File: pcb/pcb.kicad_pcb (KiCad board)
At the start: 2 copper layers, 350 x 170 mm, 79 parts, among them J1 Conn_01x24, SW1 0, SW10 9, SW11 HYPHEN, SW12 CARET, SW13 YEN, SW14 AT, SW15 LBRACKET, SW16 SEMICOLON, SW17 COLON, SW18 RBRACKET, SW19 COMMA, SW2 1, SW20 FULLSTOP, SW21 SLASH, SW22 UNDERSCORE, SW23 A, SW24 B, SW25 C, SW26 D, SW27 E, SW28 F, SW29 G, SW3 2, SW30 H, SW31 I, SW32 J, SW33 K, SW34 L, SW35 M, SW36 N, SW37 O, SW38 P, SW39 Q, SW4 3, SW40 R, SW41 PAUSE, SW42 S, SW43 T, SW44 U, SW45 V, SW46 W, SW47 X, SW48 Y, SW49 Z, SW5 4, SW50 LSHIFT, SW51 CTRL, SW52 GRAPH, SW53 CAP, SW54 KANA, SW55 F1/F6, SW56 F2/F7, SW57 F3/F8, SW58 RSHIFT, SW59 F4/F9, SW6 5, SW60 F5/F10, SW61 ESC, SW62 TAB, SW63 STOP, SW64 BS, SW65 SELECT, SW66 RETURN, SW67 SPACE, SW68 HOME, SW69 INS, SW7 6, SW70 DEL, SW71 LEFT, SW72 UP, SW73 DOWN, SW74 RIGHT, SW8 7, SW9 8

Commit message: PCB via fiducials and routing optimisations
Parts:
- turned SW64 to 45 degrees
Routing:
- net /6: track 520.4 -> 559.5 mm
- net /8: track 698.8 -> 706.0 mm
- net /17: track 473.1 -> 466.1 mm
- net /5: track 1030.1 -> 1023.3 mm
- net /9: track 765.8 -> 759.1 mm
- net /16: track 411.7 -> 418.2 mm
- net /12: track 769.5 -> 767.4 mm
- net /1: track 694.7 -> 695.6 mm
- net /7: track 692.4 -> 691.8 mm, vias 6 -> 5
- net Net-(J1-Pin_22): track 247.3 -> 246.7 mm

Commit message: Reviewing PCB and updating switch spacing
Changed soldermask layer on the connector to not be along the whole
trace. Reviewed the pinout of all the switches and confirmed they're
good. Reviewed the spacing of the switches and found errors, I have
moved them but am yet to reroute the traces. Updated the teardrops to be
curved.
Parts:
- removed SYM1: Logo_Open_Hardware_Small, Symbol:OSHW-Logo_5.7x6mm_SilkScreen
- added FID3: Fiducial, Fiducial:Fiducial_1mm_Mask2mm, F.Cu at (35.5, 211.0)
- added FID4: Fiducial, Fiducial:Fiducial_1mm_Mask2mm, B.Cu at (381.5, 211.0)
- FID1: moved to B.Cu
- moved FID1 110.0 mm to (35.5, 101.0), turned to 180 degrees
- moved SW11 0.54 mm to (260.7, 124.4)
- moved SW12 0.54 mm to (279.7, 124.4)
- moved SW13 0.54 mm to (298.8, 124.4)
- moved SW8 0.54 mm to (184.5, 124.4)
- moved SW4 0.54 mm to (108.3, 124.4)
- moved SW5 0.54 mm to (127.3, 124.4)
- moved SW1 0.54 mm to (241.6, 124.4)
- moved SW10 0.54 mm to (222.6, 124.4)
- moved SW2 0.54 mm to (70.2, 124.4)
- moved SW3 0.54 mm to (89.2, 124.4)
- moved SW6 0.54 mm to (146.4, 124.4)
- moved SW7 0.54 mm to (165.4, 124.4)
- moved SW9 0.54 mm to (203.5, 124.4)
- moved SW64 0.54 mm to (317.8, 124.4)
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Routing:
- net /16: track 418.2 -> 293.9 mm
- net /5: track 1023.3 -> 914.5 mm
- net /11: track 616.4 -> 509.1 mm, vias 6 -> 5
- net /1: track 695.6 -> 608.1 mm
- net /15: track 422.5 -> 349.9 mm, vias 5 -> 4
- net /4: track 256.2 -> 184.1 mm, vias 4 -> 3
- net /9: track 759.1 -> 692.5 mm
- net /13: track 690.9 -> 625.2 mm, vias 5 -> 4
- net /3: track 388.7 -> 325.7 mm
- net /14: track 296.4 -> 247.7 mm, vias 2 -> 1
- net /2: track 703.7 -> 663.0 mm, vias 6 -> 5
- net /10: track 583.9 -> 545.4 mm, vias 6 -> 5
- net /7: track 691.8 -> 663.6 mm
- net /17: track 466.1 -> 442.5 mm
- net /12: track 767.4 -> 745.4 mm, vias 6 -> 5
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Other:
- outline, holes or cut-outs redrawn
- rule pad_to_mask_clearance: 0 -> 0.1
- board text added: "1"
- board text added: "2"

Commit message: Rerouted the deleted traces
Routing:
- net /16: track 293.9 -> 408.0 mm
- net /5: track 914.5 -> 1023.7 mm
- net /11: track 509.1 -> 617.8 mm, vias 5 -> 6
- net /1: track 608.1 -> 698.3 mm
- net /15: track 349.9 -> 424.5 mm, vias 4 -> 5
- net /4: track 184.1 -> 258.3 mm, vias 3 -> 4
- net /13: track 625.2 -> 692.7 mm, vias 4 -> 5
- net /9: track 692.5 -> 756.7 mm
- net /3: track 325.7 -> 387.2 mm
- net /14: track 247.7 -> 299.2 mm, vias 1 -> 2
- net /2: track 663.0 -> 705.2 mm, vias 5 -> 6
- net /10: track 545.4 -> 580.4 mm, vias 5 -> 6
- net /7: track 663.6 -> 689.7 mm
- net /17: track 442.5 -> 466.5 mm
- net /12: track 745.4 -> 769.0 mm, vias 5 -> 6
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
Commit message: Adding stiffener and fab notes
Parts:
- moved D1 25.0 mm to (365.1, 129.0)
- moved FID1 25.0 mm to (35.5, 126.0)
- moved FID2 25.0 mm to (381.5, 126.5)
- moved FID3 25.0 mm to (35.5, 236.0)
- moved FID4 25.0 mm to (381.5, 236.0)
- moved J1 25.0 mm to (300.3, 86.5)
- moved SW1 25.0 mm to (241.6, 149.4)
- moved SW10 25.0 mm to (222.6, 149.4)
- moved SW11 25.0 mm to (260.7, 149.4)
- moved SW12 25.0 mm to (279.7, 149.4)
- moved SW13 25.0 mm to (298.8, 149.4)
- moved SW14 25.0 mm to (270.2, 168.4)
- moved SW15 25.0 mm to (289.3, 168.4)
- moved SW16 25.0 mm to (255.9, 187.5)
- moved SW17 25.0 mm to (275.0, 187.5)
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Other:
- rule pad_to_mask_clearance: 0.1 -> 0
- board text added: "0 mm"
- board text added: "0.0117 mm"
- board text added: "0.025 mm"
- board text added: "0.0254 um (1 u{dblquote})"
- board text added: "0.0275 mm"
- board text added: "0.1100 mm"
- board text added: "0.2500 mm"
- board text added: "0.2500 mm / 0.2500 mm"
- board text added: "0.3100 mm"
- board text added: "0.5000 mm"
- board text added: "12 um finish copper (1/3 Oz.)"
- board text added: "350.0000 mm x 170.0000 mm"
- board text added: "65.0000 mm x 15.0000 mm"
- board text added: "B.Cu"
- board text added: "B.Mask"
- board text added: "B.Paste"
- board text added: "B.Silkscreen"
- board text added: "B.Stiffener"
- board text added: "BOARD CHARACTERISTICS"
- board text added: "Blind and buried vias:"
- board text added: "Board Thickness:"
- board text added: "Board overall dimensions:"
- board text added: "Bottom Silk Screen"
- board text added: "Bottom Solder Mask"
- board text added: "Bottom Solder Paste"
- board text added: "Bottom Stiffener"
- board text added: "Castellated pads:"
- board text added: "Color"
- board text added: "Copper Finish:"
- board text added: "Copper Layer Count:"
- board text added: "Copper Thickness:"
- board text added: "Coverlay"
- board text added: "Cut-out in design:"
- board text added: "Dielectric 1"
- board text added: "Direct Printing"
- board text added: "ENIG"
- board text added: "Edge card connectors:"
- board text added: "F.Cu"
- board text added: "F.Mask"
- board text added: "F.Paste"
- board text added: "F.Silkscreen"
- board text added: "Gerber layer:"
- board text added: "Impedance Control:"
- board text added: "Layer Name"
- board text added: "Material"
- board text added: "Material:"
- board text added: "Min hole diameter:"
- board text added: "Min track/spacing:"
- board text added: "Minimum plating thickness:"
- board text added: "No"
- board text added: "Plated Board Edge:"
- board text added: "Polyimide"
- board text added: "STIFFENER CHARACTERISTICS"
- board text added: "Stiffener Thickness:"
- board text added: "Stiffener overall dimensions:"
- board text added: "Stiffener required:"
- board text added: "Tented"
- board text added: "Thickness (mm)"
- board text added: "Top Silk Screen"
- board text added: "Top Solder Mask"
- board text added: "Top Solder Paste"
- board text added: "Total Thickness:"
- board text added: "Type"
- board text added: "User.1"
- board text added: "Via covering:"
- board text added: "Via in pad:"
- board text added: "White"
- board text added: "Yellow"
- board text added: "Yes"
- board text added: "copper"
- board text added: "core"

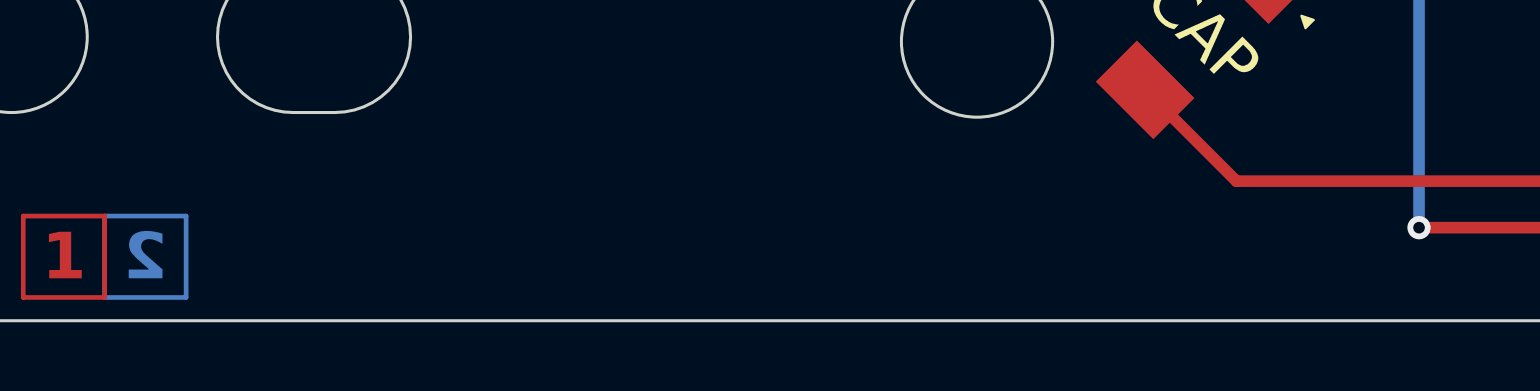
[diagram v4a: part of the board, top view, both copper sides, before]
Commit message: Adding serial number label
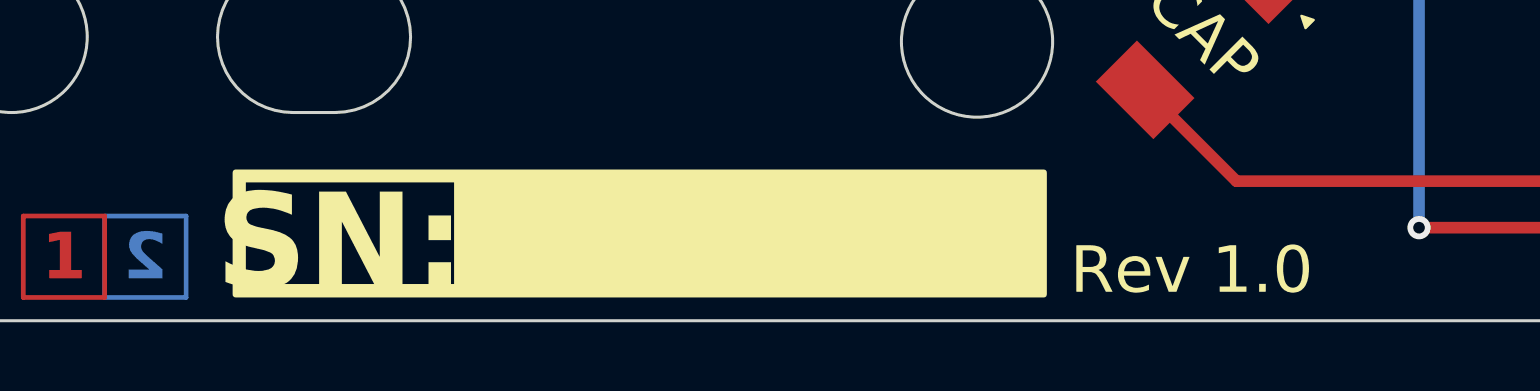
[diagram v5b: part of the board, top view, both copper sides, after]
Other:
- board text added: "Colour"
- board text added: "Rev 1.0"
- board text added: "SN:"
- board text removed: "Color"

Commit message: Reworked PCB and stiffener thickness
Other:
- board text added: "0.1034 mm"
- board text added: "0.2250 mm"
- board text added: "0.2892 mm"
- board text added: "Copper on stiffener side:"
- board text removed: "0.1100 mm"
- board text removed: "0.2500 mm"
- board text removed: "0.3100 mm"
